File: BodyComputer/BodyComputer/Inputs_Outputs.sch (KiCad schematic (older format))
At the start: 111 parts

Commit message: Update due to moving to another computer. Updated Schematic, Print-outs, PCB in development
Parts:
- removed J?: Screw_Terminal_01x02, SamacSys_Parts:SHDR2W99P0X500_1X2_1000X760X1000P, symbol Connector:Screw_Terminal_01x02
- added D56, D57: D_Zener, Diode_SMD:D_SOD-323_HandSoldering, symbol Device:D_Zener
- added J21: Screw_Terminal_01x02, SamacSys_Parts:SHDR2W99P0X500_1X2_1000X760X1000P, symbol Connector:Screw_Terminal_01x02
- added R101, R30, R31, R44, R45, R46, R47, R58, R59, R60, R65, R66, R80, R84, R89, R90: 10k, Resistor_SMD:R_0603_1608Metric, symbol Device:R
- added R160, R161, R7, R8: 0, Resistor_SMD:R_0603_1608Metric, symbol Device:R
- D12, D13, D14, D15, D16, D17, D18, D19, D20, D21, D22, D25, D29, D30, D31, D35: renamed from D?; footprint Diode_SMD:D_0603_1608Metric -> Diode_SMD:D_SMA
- D23, D24, D26, D27, D28, D32, D33, D34: renamed from D?; footprint (none) -> Diode_SMD:D_SOD-323_HandSoldering
- J22, J25: renamed from J?; footprint (none) -> SamacSys_Parts:SHDR3W95P0X500_1X3_1620X900X1280P
- U6: renamed from U?; footprint (none) -> Package_DIP:DIP-8_W7.62mm_Socket_LongPads
- gave numbers to parts that had none: 82
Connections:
- net GND: now also D56.2 (A), D57.2 (A), R101.1, R160.1, R161.2, R30.2, R31.2, R44.1, R45.1, R46.2, R47.2, R58.1, R59.1, R60.2, R65.1, R66.2, R80.1, R84.2, R89.1, R90.2
- net MOSFET_OUT_13: now also R35.2; no longer R35.1
- net MOSFET_OUT_15: now also R53.2; no longer R53.1
- net at Q2.1 (G), R32.1: now also R30.1
- net at Q4.1 (G), R38.1: now also R44.2
- net at Q6.1 (G), R50.1: now also R46.1
- net at Q8.1 (G), R56.1: now also R59.2
- net at Q10.1 (G), R61.1: now also R60.1
- net at Q11.1 (G), R64.1: now also R65.2
- net at Q12.1 (G), R71.1: now also R66.1
- net at Q13.1 (G), R79.1: now also R80.2
- net at Q14.1 (G), R85.1: now also R84.1
- net at Q15.1 (G), R88.1: now also R89.2
- net at Q16.1 (G), R91.1: now also R90.1
- net at Q17.1 (G), R100.1: now also R101.2
- net at Q3.1 (G), R33.1: now also R31.1
- net at D13.1 (K), J16.1 (Pin_1), Q3.3 (D): now also R35.1; no longer R35.2
- net at Q5.1 (G), R39.1: now also R45.2
- net at Q7.1 (G), R51.1: now also R47.1
- net at D17.1 (K), J18.1 (Pin_1), Q7.3 (D): now also R53.1; no longer R53.2
- net at Q9.1 (G), R57.1: now also R58.2
- net at J19.1 (Pin_1), R48.2, U6.1: now also R68.2
- net at J19.2 (Pin_2), R49.2, U6.7: now also R69.1
- new net: J21.2 (Pin_2), R7.2
- new net: J21.1 (Pin_1), R8.1
- new net ADC_7: D56.1 (K), R160.2, R7.1
- new net ADC_8: D57.1 (K), R161.1, R8.2
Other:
- moved on the sheet: D12, D13, D14, D15, D16, D17, D18, D19, D20, D21, D22, D23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

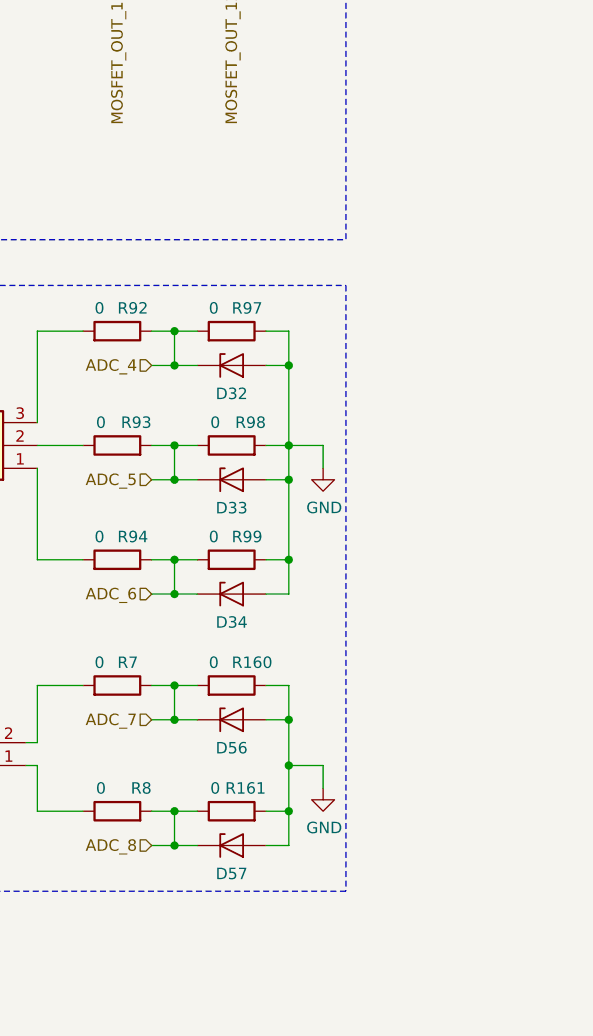
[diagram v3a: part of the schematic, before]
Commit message: Body Computer [DONE]
Body Computer done as a 2-layer board and put into prototype production, schematics and PCBs created.
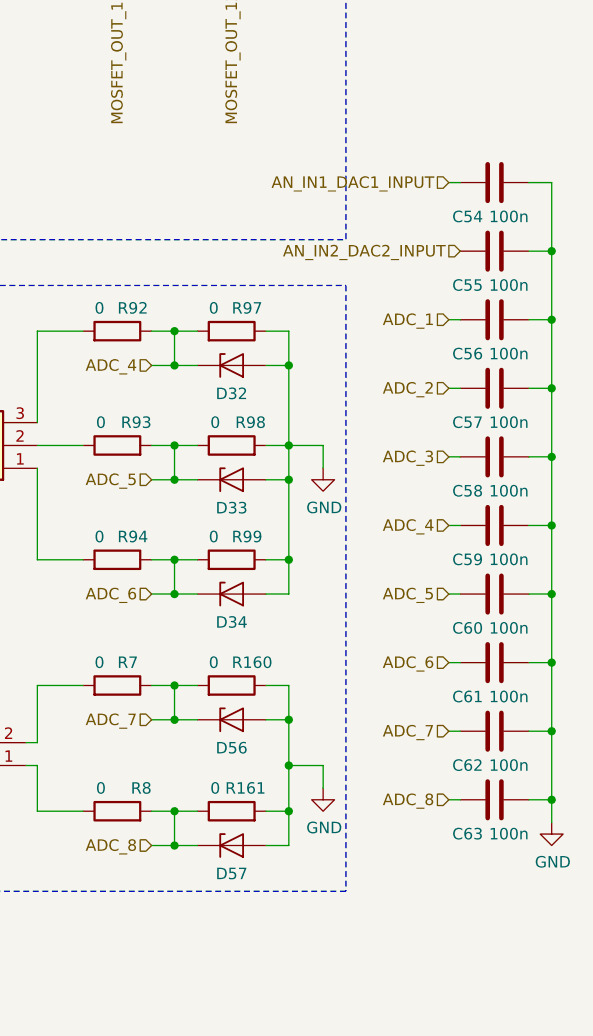
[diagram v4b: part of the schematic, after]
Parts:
- added C54, C55, C56, C57, C58, C59, C60, C61, C62, C63: 100n, Capacitor_SMD:C_0603_1608Metric, symbol Device:C
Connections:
- net ADC_1: now also C56.2
- net ADC_2: now also C57.2
- net ADC_3: now also C58.2
- net ADC_4: now also C59.2
- net ADC_5: now also C60.2
- net ADC_6: now also C61.2
- net ADC_7: now also C62.2
- net ADC_8: now also C63.2
- net AN_IN1_DAC1_INPUT: now also C54.2
- net AN_IN2_DAC2_INPUT: now also C55.2
- net GND: now also C54.1, C55.1, C56.1, C57.1, C58.1, C59.1, C60.1, C61.1, C62.1, C63.1
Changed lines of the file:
@@
 Sheet 5 7
 Title "Body Computer"
-Date "2020-04-12"
+Date "2020-04-17"
 Rev "1.0"
 Comp "Wojciech Grzeliński"
@@
 Wire Notes Line
 	9850 3800 9850 6450
+$Comp
+L Device:C C56
+U 1 1 5E9C969B
+P 10500 3950
+F 0 "C56" V 10350 3900 50  0000 R CNN
+F 1 "100n" V 10350 4100 50  0000 R CNN
+F 2 "Capacitor_SMD:C_0603_1608Metric" H 10538 3800 50  0001 C CNN
+F 3 "~" H 10500 3950 50  0001 C CNN
+	1    10500 3950
+	0    1    -1   0
+$EndComp
+$Comp
+L Device:C C57
+U 1 1 5E9CD2B3
+P 10500 4250
+F 0 "C57" V 10350 4200 50  0000 R CNN
+F 1 "100n" V 10350 4400 50  0000 R CNN
+F 2 "Capacitor_SMD:C_0603_1608Metric" H 10538 4100 50  0001 C CNN
+F 3 "~" H 10500 4250 50  0001 C CNN
+	1    10500 4250
+	0    1    -1   0
+$EndComp
+$Comp
+L Device:C C58
+U 1 1 5E9F569A
+P 10500 4550
+F 0 "C58" V 10350 4500 50  0000 R CNN
+F 1 "100n" V 10350 4700 50  0000 R CNN
+F 2 "Capacitor_SMD:C_0603_1608Metric" H 10538 4400 50  0001 C CNN
+F 3 "~" H 10500 4550 50  0001 C CNN
+	1    10500 4550
+	0    1    -1   0
+$EndComp
+Text HLabel 10300 3950 0    50   Input ~ 0
+ADC_1
+Text HLabel 10300 4250 0    50   Input ~ 0
+ADC_2
+Text HLabel 10300 4550 0    50   Input ~ 0
+ADC_3
+Wire Wire Line
+	10350 4550 10300 4550
+Wire Wire Line
+	10350 4250 10300 4250
+Wire Wire Line
+	10350 3950 10300 3950
+$Comp
+L Device:C C59
+U 1 1 5EC43021
+P 10500 4850
+F 0 "C59" V 10350 4800 50  0000 R CNN
+F 1 "100n" V 10350 5000 50  0000 R CNN
+F 2 "Capacitor_SMD:C_0603_1608Metric" H 10538 4700 50  0001 C CNN
+F 3 "~" H 10500 4850 50  0001 C CNN
+	1    10500 4850
+	0    1    -1   0
+$EndComp
+$Comp
+L Device:C C60
+U 1 1 5EC43027
+P 10500 5150
+F 0 "C60" V 10350 5100 50  0000 R CNN
+F 1 "100n" V 10350 5300 50  0000 R CNN
+F 2 "Capacitor_SMD:C_0603_1608Metric" H 10538 5000 50  0001 C CNN
+F 3 "~" H 10500 5150 50  0001 C CNN
+	1    10500 5150
+	0    1    -1   0
+$EndComp
+$Comp
+L Device:C C61
+U 1 1 5EC4302D
+P 10500 5450
+F 0 "C61" V 10350 5400 50  0000 R CNN
+F 1 "100n" V 10350 5600 50  0000 R CNN
+F 2 "Capacitor_SMD:C_0603_1608Metric" H 10538 5300 50  0001 C CNN
+F 3 "~" H 10500 5450 50  0001 C CNN
+	1    10500 5450
+	0    1    -1   0
+$EndComp
+Wire Wire Line
+	10350 5450 10300 5450
+Wire Wire Line
+	10350 5150 10300 5150
+Wire Wire Line
+	10350 4850 10300 4850
+$Comp
+L Device:C C62
+U 1 1 5EC6CDD9
+P 10500 5750
+F 0 "C62" V 10350 5700 50  0000 R CNN
+F 1 "100n" V 10350 5900 50  0000 R CNN
+F 2 "Capacitor_SMD:C_0603_1608Metric" H 10538 5600 50  0001 C CNN
+F 3 "~" H 10500 5750 50  0001 C CNN
+	1    10500 5750
+	0    1    -1   0
+$EndComp
+$Comp
+L Device:C C63
+U 1 1 5EC6CDDF
+P 10500 6050
+F 0 "C63" V 10350 6000 50  0000 R CNN
+F 1 "100n" V 10350 6200 50  0000 R CNN
+F 2 "Capacitor_SMD:C_0603_1608Metric" H 10538 5900 50  0001 C CNN
+F 3 "~" H 10500 6050 50  0001 C CNN
+	1    10500 6050
+	0    1    -1   0
+$EndComp
+$Comp
+L Device:C C54
+U 1 1 5EC6CDE5
+P 10500 3350
+F 0 "C54" V 10350 3300 50  0000 R CNN
+F 1 "100n" V 10350 3500 50  0000 R CNN
+F 2 "Capacitor_SMD:C_0603_1608Metric" H 10538 3200 50  0001 C CNN
+F 3 "~" H 10500 3350 50  0001 C CNN
+	1    10500 3350
+	0    1    -1   0
+$EndComp
+Wire Wire Line
+	10350 3350 10300 3350
+Wire Wire Line
+	10350 6050 10300 6050
+Wire Wire Line
+	10350 5750 10300 5750
+Text HLabel 10300 4850 0    50   Input ~ 0
+ADC_4
+Text HLabel 10300 5150 0    50   Input ~ 0
+ADC_5
+Text HLabel 10300 5450 0    50   Input ~ 0
+ADC_6
+Text HLabel 10300 5750 0    50   Input ~ 0
+ADC_7
+Text HLabel 10300 6050 0    50   Input ~ 0
+ADC_8
+Text HLabel 10300 3350 0    50   Input ~ 0
+AN_IN1_DAC1_INPUT
+Text HLabel 10350 3650 0    50   Input ~ 0
+AN_IN2_DAC2_INPUT
+$Comp
+L Device:C C55
+U 1 1 5EDE7F2F
+P 10500 3650
+F 0 "C55" V 10350 3600 50  0000 R CNN
+F 1 "100n" V 10350 3800 50  0000 R CNN
+F 2 "Capacitor_SMD:C_0603_1608Metric" H 10538 3500 50  0001 C CNN
+F 3 "~" H 10500 3650 50  0001 C CNN
+	1    10500 3650
+	0    1    -1   0
+$EndComp
+Wire Wire Line
+	10650 3950 10750 3950
+Wire Wire Line
+	10750 3950 10750 4250
+Wire Wire Line
+	10750 4250 10650 4250
+Wire Wire Line
+	10650 6050 10750 6050
+Wire Wire Line
+	10750 6050 10750 5750
+Wire Wire Line
+	10750 5750 10650 5750
+Wire Wire Line
+	10750 5750 10750 5450
+Wire Wire Line
+	10750 5450 10650 5450
+Connection ~ 10750 5750
+Wire Wire Line
+	10750 5450 10750 5150
+Wire Wire Line
+	10750 5150 10650 5150
+Connection ~ 10750 5450
+Wire Wire Line
+	10750 5150 10750 4850
+Wire Wire Line
+	10750 4850 10650 4850
+Connection ~ 10750 5150
+Wire Wire Line
+	10750 4850 10750 4550
+Wire Wire Line
+	10750 4550 10650 4550
+Connection ~ 10750 4850
+Wire Wire Line
+	10750 4550 10750 4250
+Connection ~ 10750 4550
+Connection ~ 10750 4250
+$Comp
+L power:GND #PWR?
+U 1 1 5F01FAA2
+P 10750 6150
+AR Path="/5F25F1A8/5F01FAA2" Ref="#PWR?"  Part="1"
+AR Path="/5E6DC799/5F01FAA2" Ref="#PWR?"  Part="1"
+AR Path="/5E667041/5F01FAA2" Ref="#PWR?"  Part="1"
+AR Path="/5E6671BF/5F01FAA2" Ref="#PWR?"  Part="1"
+AR Path="/5E731526/5F01FAA2" Ref="#PWR0147"  Part="1"
+F 0 "#PWR0147" H 10750 5900 50  0001 C CNN
+F 1 "GND" H 10755 5977 50  0000 C CNN
+F 2 "" H 10750 6150 50  0001 C CNN
+F 3 "" H 10750 6150 50  0001 C CNN
+	1    10750 6150
+	1    0    0    -1
+$EndComp
+Connection ~ 10750 6050
+Wire Wire Line
+	10750 3950 10750 3650
+Wire Wire Line
+	10750 3650 10650 3650
+Connection ~ 10750 3950
+Wire Wire Line
+	10750 3650 10750 3350
+Wire Wire Line
+	10750 3350 10650 3350
+Connection ~ 10750 3650
+Wire Wire Line
+	10750 6050 10750 6150
 $EndSCHEMATC
